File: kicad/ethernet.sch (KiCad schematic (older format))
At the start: 37 parts, among them U2 NUP4114UPXV6T1G, U3 NUP4114UPXV6T1G, X1 L829-1J1T-43

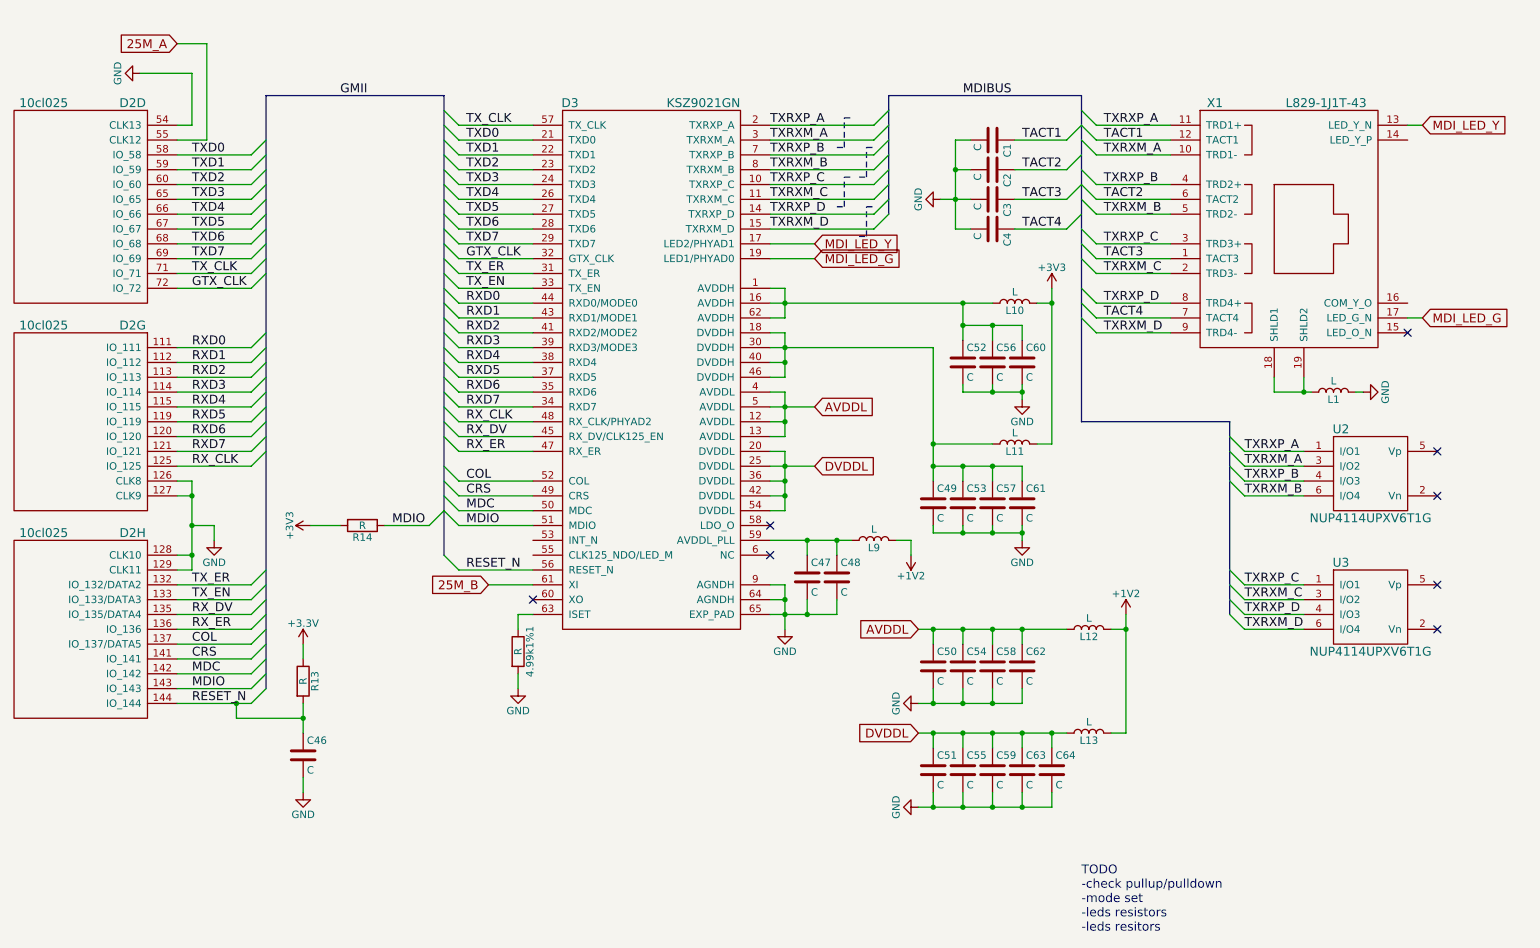
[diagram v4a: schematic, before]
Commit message: finished electrical connections
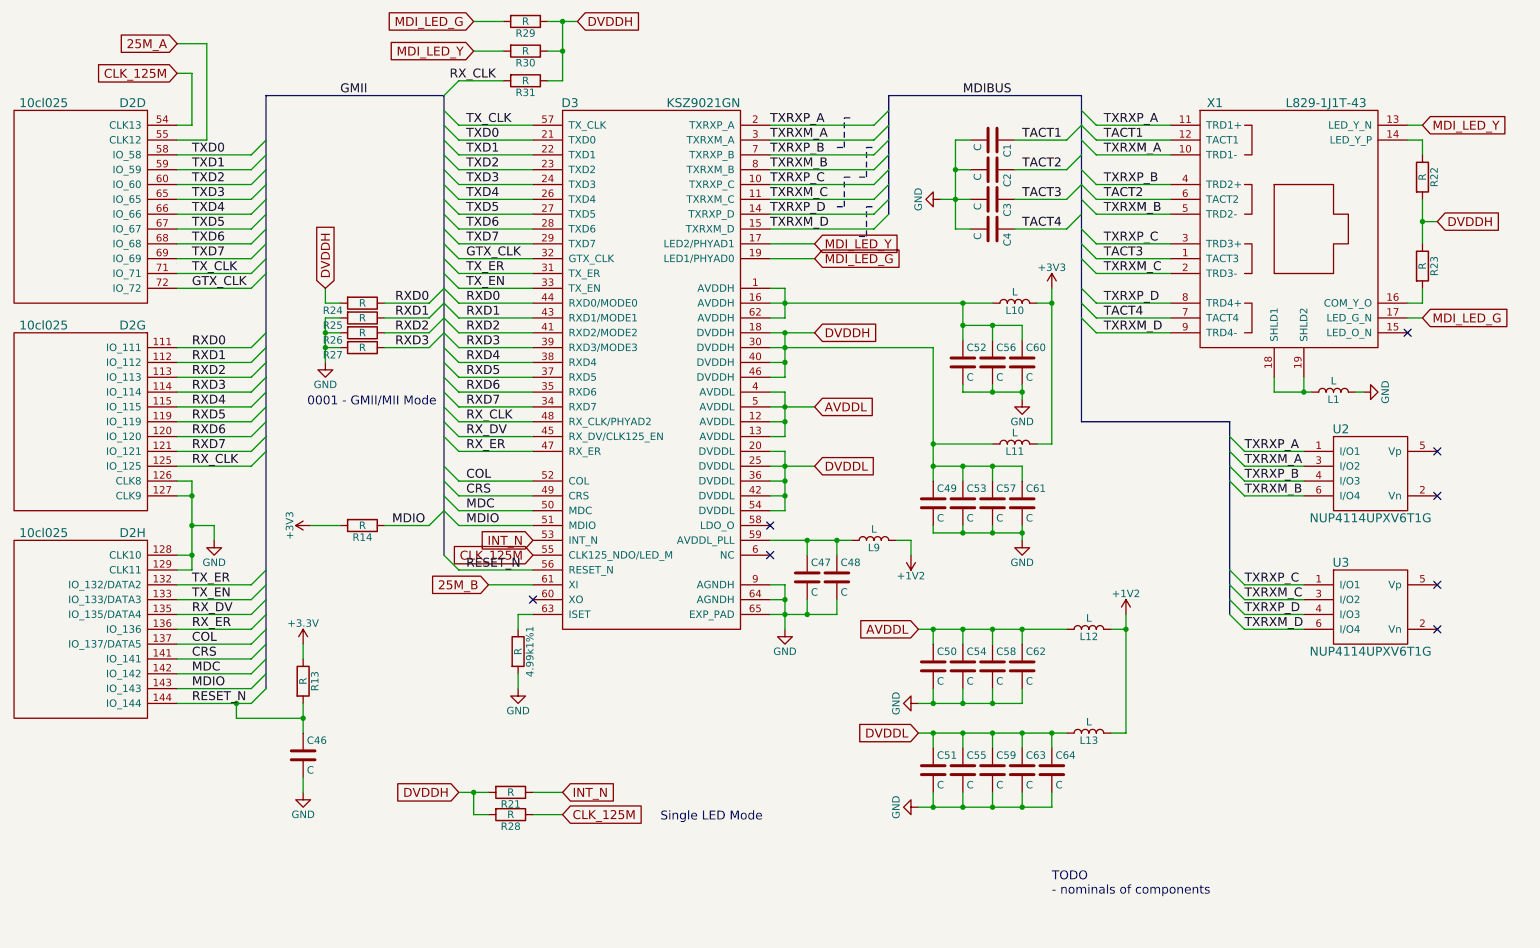
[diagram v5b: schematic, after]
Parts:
- added R21, R22, R23, R24, R25, R26, R27, R28, R29, R30, R31: R, symbol R
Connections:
- net GND: now also R25.2, R26.2, R27.2; no longer D2.54 (CLK13)
- net MDI_LED_G: now also R29.2
- net MDI_LED_Y: now also R30.2
- net RXD0: now also R24.1
- net RXD1: now also R25.1
- net RXD2: now also R26.1
- net RXD3: now also R27.1
- net RX_CLK: now also R31.2
- net at X1.14 (LED_Y_P): now also R22.1
- net at X1.16 (COM_Y_O): now also R23.2
- net DVDDH: now reaches C49.1, C53.1, C57.1, C61.1, D3.18 (DVDDH), D3.30 (DVDDH), D3.40 (DVDDH), D3.46 (DVDDH), L11.1
- net DVDDH: now also R21.2, R22.2, R23.1, R24.2, R28.2, R29.1, R30.1, R31.1
- net INT_N: now reaches D3.53 (INT_N)
- net INT_N: now also R21.1
- net CLK_125M: now reaches D3.55 (CLK125_NDO/LED_M)
- net CLK_125M: now also D2.54 (CLK13), R28.1
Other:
- note added: "0001 - GMII/MII Mode"
- note added: "Single LED Mode"
- note added: "TODO \n- nominals of components"
- note removed: "TODO \n-check pullup/pulldown\n-mode set\n-leds resistors\n-leds resitors"

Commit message: write nominal of components
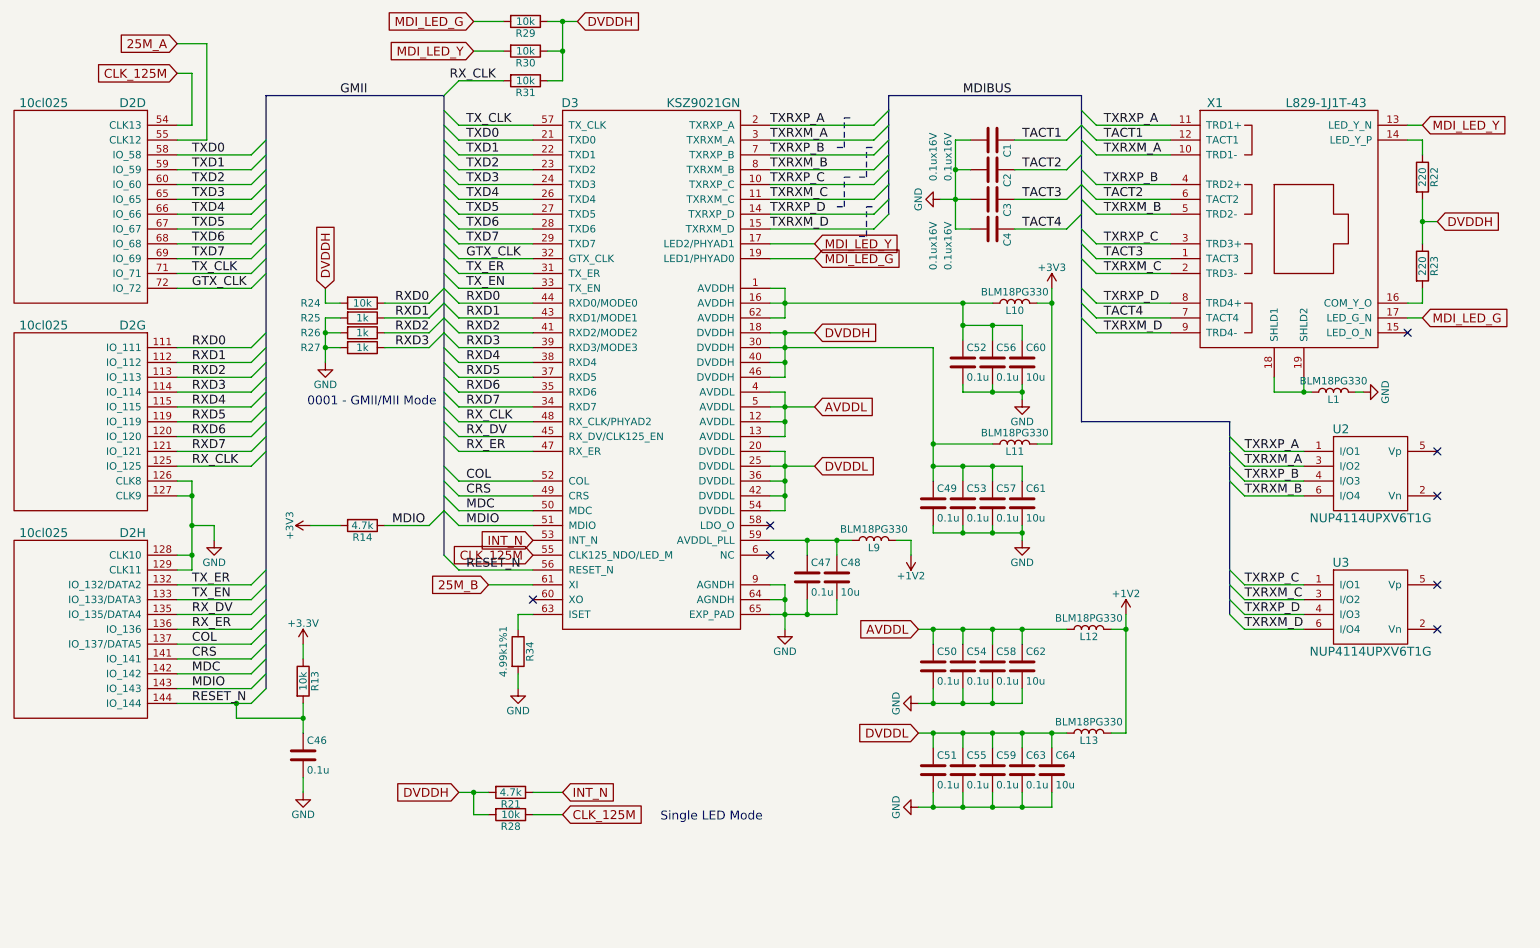
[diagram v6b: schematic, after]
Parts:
- C1, C2, C3, C4: value C -> 0.1ux16V
- C46, C47, C49, C50, C51, C52, C53, C54, C55, C56, C57, C58, C59, C63: value C -> 0.1u
- C48, C60, C61, C62, C64: value C -> 10u
- L1, L10, L11, L12, L13, L9: value L -> BLM18PG330
- R13, R24, R28, R29, R30, R31: value R -> 10k; footprint (none) -> Resistors_SMD:R_0603_HandSoldering
- R14, R21: value R -> 4.7k; footprint (none) -> Resistors_SMD:R_0603_HandSoldering
- R22, R23: value R -> 220; footprint (none) -> Resistors_SMD:R_0603_HandSoldering
- R25, R26, R27: value R -> 1k; footprint (none) -> Resistors_SMD:R_0603_HandSoldering
- R34: renamed from 4.99k1%1; value R -> 4.99k1%1
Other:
- note removed: "TODO \n- nominals of components"
